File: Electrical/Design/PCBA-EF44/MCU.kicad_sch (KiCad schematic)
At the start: 57 parts, among them J701 Conn_Coaxial, J702 (NF), J799 Conn_01x02, SW701 C255807, SW702 C2905169, SW703 C2905169, U703 RP2040, U704 ESP32-S3FN8, U705 W25Q64JVSSIQ, Y701 ESP32_XTAL

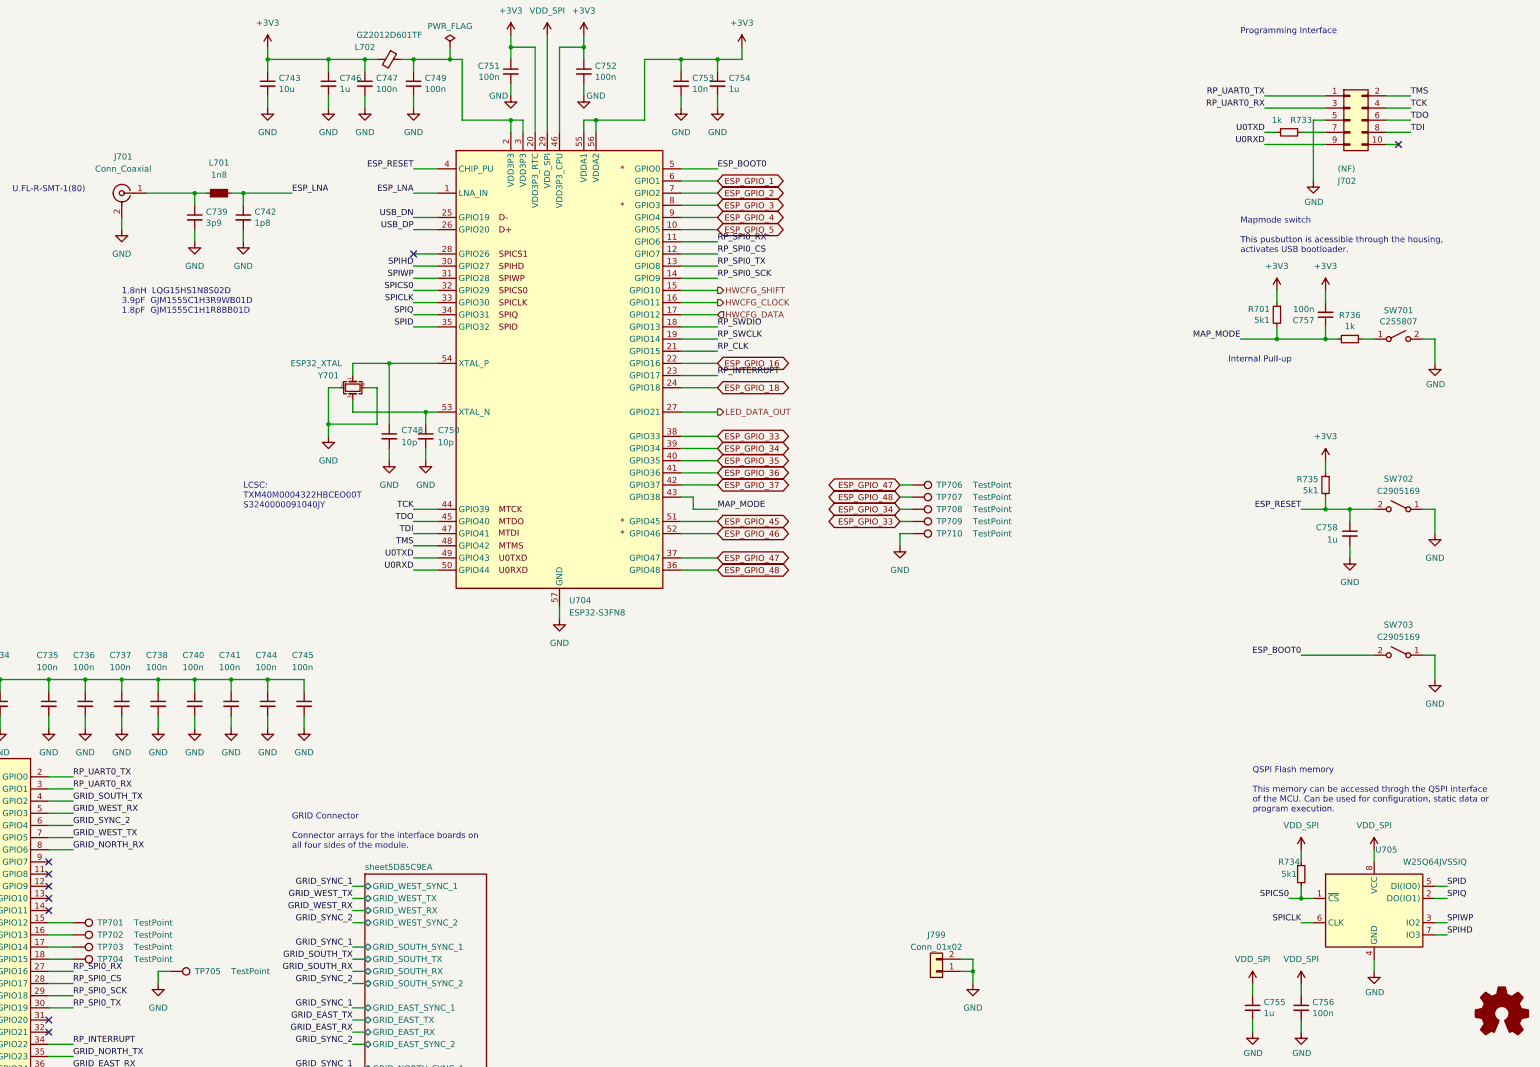
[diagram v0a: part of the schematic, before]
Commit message: SUKU pcbs updated with footprint and symbol values
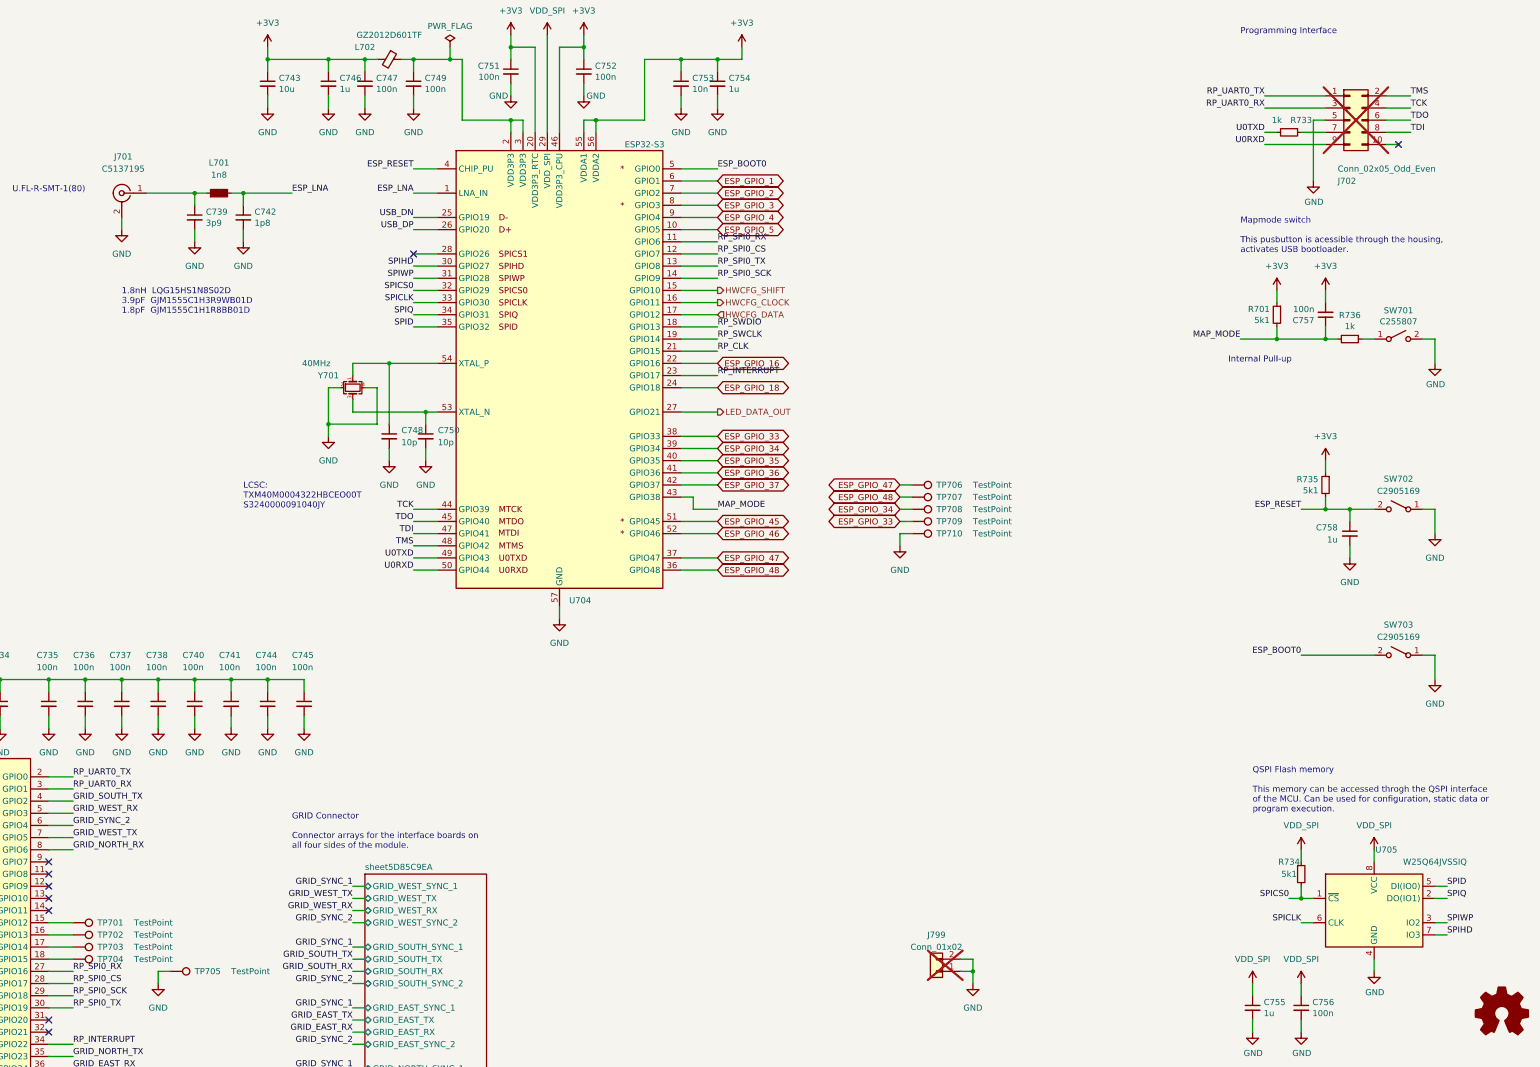
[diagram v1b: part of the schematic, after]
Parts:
- J701: value Conn_Coaxial -> C5137195
- J702: value (NF) -> Conn_02x05_Odd_Even; now not fitted; now left out of the parts list
- J799: now not fitted; now left out of the parts list
- U704: value ESP32-S3FN8 -> ESP32-S3; symbol suku_basics:ESP32-S3FN8 -> suku_basics:ESP32-S3
- Y701: value ESP32_XTAL -> 40MHz

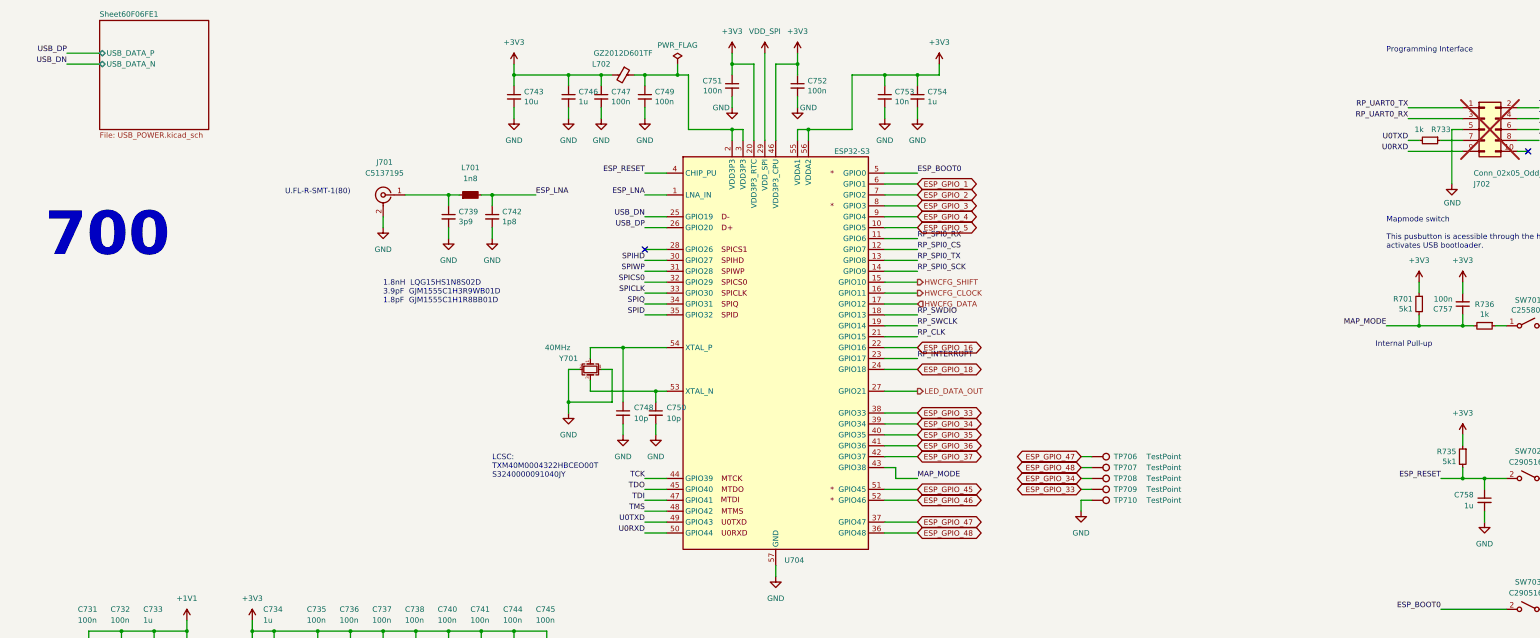
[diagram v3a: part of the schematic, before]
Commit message: SUKU debug adapter support added for EF44
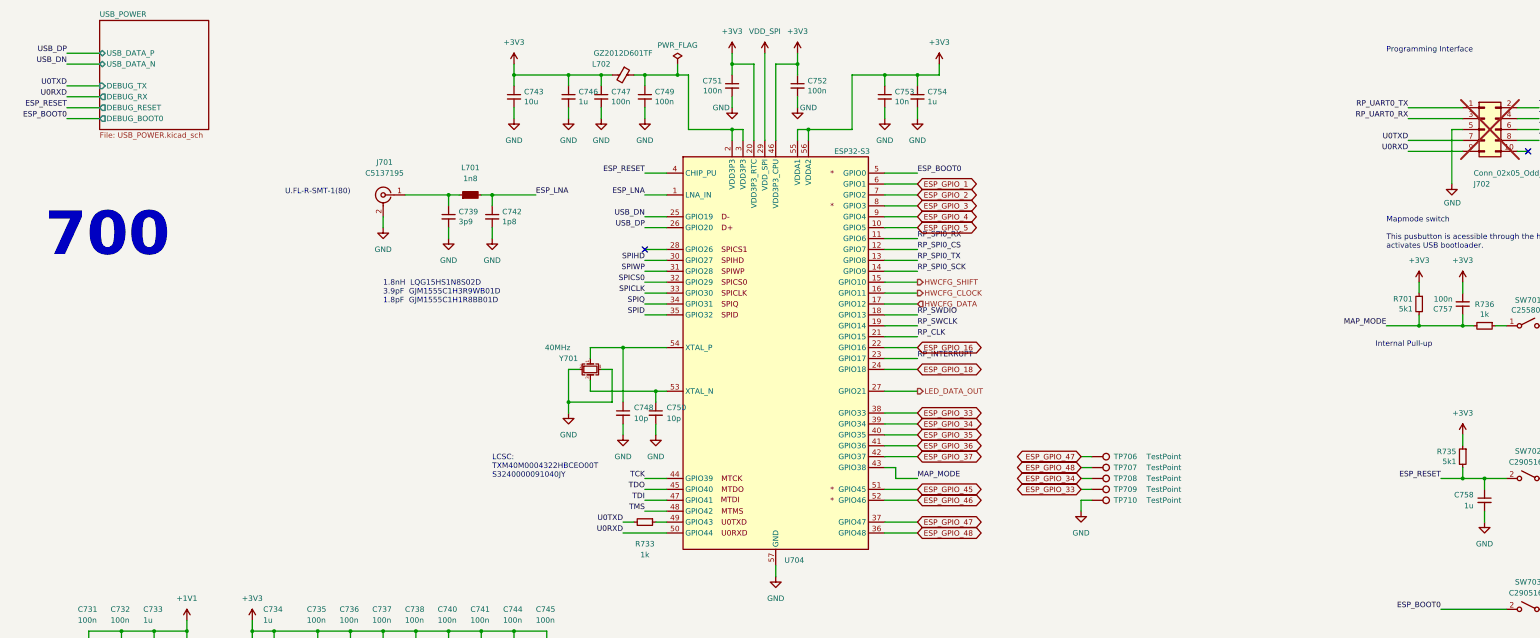
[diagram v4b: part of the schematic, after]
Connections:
- net U0TXD: now also J702.7 (Pin_7); no longer U704.49 (GPIO43)
- net at R733.1: now also U704.49 (GPIO43); no longer J702.7 (Pin_7)
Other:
- removed sheet Sheet60F06FE1
- added sheet USB_POWER (USB_POWER.kicad_sch)
- moved on the sheet: R733
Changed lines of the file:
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@@
 	(wire
 		(pts
-			(xy 345.44 53.34) (xy 342.9 53.34)
+			(xy 342.9 53.34) (xy 355.6 53.34)
 		)
 		(stroke
@@
 	(wire
 		(pts
+			(xy 30.48 40.64) (xy 38.1 40.64)
+		)
+		(stroke
+			(width 0)
+			(type default)
+		)
+	)
+	(wire
+		(pts
 			(xy 88.9 187.96) (xy 93.98 187.96)
 		)
@@
 	(wire
 		(pts
-			(xy 165.1 142.24) (xy 170.18 142.24)
+			(xy 167.64 142.24) (xy 170.18 142.24)
 		)
 		(stroke
@@
 	(wire
 		(pts
-			(xy 165.1 144.78) (xy 170.18 144.78)
+			(xy 30.48 35.56) (xy 38.1 35.56)
 		)
 		(stroke
@@
 	(wire
 		(pts
+			(xy 38.1 33.02) (xy 30.48 33.02)
+		)
+		(stroke
+			(width 0)
+			(type default)
+		)
+	)
+	(wire
+		(pts
 			(xy 35.56 256.54) (xy 38.1 256.54)
 		)
@@
 	(wire
 		(pts
+			(xy 160.02 144.78) (xy 170.18 144.78)
+		)
+		(stroke
+			(width 0)
+			(type default)
+		)
+	)
+	(wire
+		(pts
 			(xy 88.9 251.46) (xy 93.98 251.46)
 		)
@@
 	(wire
 		(pts
+			(xy 30.48 43.18) (xy 38.1 43.18)
+		)
+		(stroke
+			(width 0)
+			(type default)
+		)
+	)
+	(wire
+		(pts
 			(xy 88.9 256.54) (xy 93.98 256.54)
 		)
@@
 	(wire
 		(pts
-			(xy 355.6 53.34) (xy 350.52 53.34)
+			(xy 30.48 48.26) (xy 38.1 48.26)
 		)
 		(stroke
@@
 	(wire
 		(pts
+			(xy 160.02 142.24) (xy 162.56 142.24)
+		)
+		(stroke
+			(width 0)
+			(type default)
+		)
+	)
+	(wire
+		(pts
 			(xy 378.46 132.08) (xy 375.92 132.08)
 		)
@@
 	(wire
 		(pts
+			(xy 30.48 45.72) (xy 38.1 45.72)
+		)
+		(stroke
+			(width 0)
+			(type default)
+		)
+	)
+	(wire
+		(pts
 			(xy 220.98 81.28) (xy 228.6 81.28)
 		)
@@
 	(wire
 		(pts
-			(xy 38.1 33.02) (xy 30.48 33.02)
-		)
-		(stroke
-			(width 0)
-			(type default)
-		)
-	)
-	(wire
-		(pts
 			(xy 220.98 111.76) (xy 228.6 111.76)
 		)
@@
 	(wire
 		(pts
-			(xy 30.48 35.56) (xy 38.1 35.56)
-		)
-		(stroke
-			(width 0)
-			(type default)
-		)
-	)
-	(wire
-		(pts
 			(xy 220.98 66.04) (xy 228.6 66.04)
 		)
@@
 	)
 	(label "U0TXD"
-		(at 165.1 142.24 180)
+		(at 160.02 142.24 180)
 		(effects
 			(font
@@
 	)
 	(label "U0RXD"
-		(at 165.1 144.78 180)
+		(at 160.02 144.78 180)
 		(effects
 			(font
@@
 		)
 	)
+	(label "USB_DP"
+		(at 30.48 33.02 180)
+		(effects
+			(font
+				(size 1.27 1.27)
+			)
+			(justify right bottom)
+		)
+	)
 	(label "GRID_SOUTH_RX"
 		(at 93.98 259.08 0)
@@
 		)
 	)
-	(label "RP_SPI0_SCK"
-		(at 228.6 83.82 0)
+	(label "USB_DN"
+		(at 30.48 35.56 180)
 		(effects
 			(font
 				(size 1.27 1.27)
 			)
-			(justify left bottom)
+			(justify right bottom)
 		)
 	)
-	(label "GRID_EAST_RX"
-		(at 93.98 248.92 0)
+	(label "RP_SPI0_SCK"
+		(at 228.6 83.82 0)
 		(effects
 			(font
@@
 		)
 	)
-	(label "USB_DN"
-		(at 165.1 71.12 180)
+	(label "GRID_EAST_RX"
+		(at 93.98 248.92 0)
 		(effects
 			(font
 				(size 1.27 1.27)
 			)
-			(justify right bottom)
+			(justify left bottom)
 		)
 	)
 	(label "USB_DN"
-		(at 30.48 35.56 180)
+		(at 165.1 71.12 180)
 		(effects
 			(font
@@
 		)
 	)
+	(label "ESP_BOOT0"
+		(at 30.48 48.26 180)
+		(effects
+			(font
+				(size 1.27 1.27)
+			)
+			(justify right bottom)
+		)
+	)
 	(label "GRID_EAST_RX"
 		(at 152.4 241.3 180)
@@
 		)
 	)
+	(label "U0RXD"
+		(at 30.48 43.18 180)
+		(effects
+			(font
+				(size 1.27 1.27)
+			)
+			(justify right bottom)
+		)
+	)
 	(label "GRID_SOUTH_TX"
 		(at 93.98 193.04 0)
@@
 		)
 	)
+	(label "ESP_RESET"
+		(at 30.48 45.72 180)
+		(effects
+			(font
+				(size 1.27 1.27)
+			)
+			(justify right bottom)
+		)
+	)
 	(label "RP_CLK"
 		(at 228.6 99.06 0)
@@
 		)
 	)
-	(label "USB_DP"
-		(at 30.48 33.02 180)
-		(effects
-			(font
-				(size 1.27 1.27)
-			)
-			(justify right bottom)
-		)
-	)
 	(label "SPICLK"
 		(at 165.1 88.9 180)
@@
 		)
 	)
+	(label "U0TXD"
+		(at 30.48 40.64 180)
+		(effects
+			(font
+				(size 1.27 1.27)
+			)
+			(justify right bottom)
+		)
+	)
 	(label "SPIWP"
 		(at 381 218.44 0)
@@
 	(symbol
 		(lib_id "suku_basics:RES")
-		(at 347.98 53.34 270)
+		(at 165.1 142.24 270)
 		(unit 1)
 		(exclude_from_sim no)
@@
 		(dnp no)
 		(property "Reference" "R733"
-			(at 350.52 50.8 90)
+			(at 165.1 147.32 90)
 			(effects
 				(font
@@
 		)
 		(property "Value" "1k"
-			(at 345.44 50.8 90)
+			(at 165.1 149.86 90)
 			(effects
 				(font
@@
 		)
 		(property "Footprint" "suku_basics:RES_0402"
-			(at 347.98 53.34 0)
+			(at 165.1 142.24 0)
 			(effects
 				(font
@@
 		)
 		(property "Datasheet" "~"
-			(at 347.98 53.34 0)
+			(at 165.1 142.24 0)
 			(effects
 				(font
@@
 		)
 		(property "Description" ""
-			(at 347.98 53.34 0)
+			(at 165.1 142.24 0)
 			(effects
 				(font
@@
 			(color 0 0 0 0.0000)
 		)
-		(property "Sheetname" "Sheet60F06FE1"
+		(property "Sheetname" "USB_POWER"
 			(at 38.1 24.6884 0)
 			(effects
@@
 			)
 		)
+		(pin "DEBUG_TX" input
+			(at 38.1 40.64 180)
+			(effects
+				(font
+					(size 1.27 1.27)
+				)
+				(justify left)
+			)
+		)
+		(pin "DEBUG_RX" output
+			(at 38.1 43.18 180)
+			(effects
+				(font
+					(size 1.27 1.27)
+				)
+				(justify left)
+			)
+		)
+		(pin "DEBUG_RESET" output
+			(at 38.1 45.72 180)
+			(effects
+				(font
+					(size 1.27 1.27)
+				)
+				(justify left)
+			)
+		)
+		(pin "DEBUG_BOOT0" output
+			(at 38.1 48.26 180)
+			(effects
+				(font
+					(size 1.27 1.27)
+				)
+				(justify left)
+			)
+		)
 		(instances
 			(project "PCBA-EF44"
 				(path "/e5217a0c-7f55-4c30-adda-7f8d95709d1b/00000000-0000-0000-0000-00005d757c78"
-					(page "9")
+					(page "2")
 				)
 			)

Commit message: SUKU reset and boot button footprints updated
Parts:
- SW702, SW703: footprint Button_Switch_SMD:SW_SPST_CK_RS282G05A3 -> suku_basics:SW_SPST_CK_RS282G05A3
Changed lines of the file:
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@@
 			)
 		)
-		(property "Footprint" "Button_Switch_SMD:SW_SPST_CK_RS282G05A3"
+		(property "Footprint" "suku_basics:SW_SPST_CK_RS282G05A3"
 			(at 370.84 132.08 0)
 			(effects
@@
 			)
 		)
-		(property "Footprint" "Button_Switch_SMD:SW_SPST_CK_RS282G05A3"
+		(property "Footprint" "suku_basics:SW_SPST_CK_RS282G05A3"
 			(at 370.84 162.56 0)
 			(effects
